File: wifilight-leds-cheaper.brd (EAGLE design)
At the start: 50.8 x 50.8 mm, 51 parts, among them Q1 BUK98180-100A, Q2 BUK98180-100A, Q3 BUK98180-100A, Q4 BUK98180-100A, U2 PCA9685

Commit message: add GPIO2 pins pogopins for programming
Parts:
- added TPCHPD, TPGPIO2: TEST-POINT3X5, SparkFun-Passives:PAD.03X.05
- moved TPGPIO0 1.11 mm to (26.2, 27.6)
- moved R5 0.16 mm to (28.4, 34.8)
- moved R6 0.16 mm to (30.5, 34.8)
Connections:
- removed net N$27: MPU.11
- removed net N$34: MPU.3
- new net CH_PD: MPU.11, TPCHPD.P$1
- new net GPIO2: MPU.3, TPGPIO2.P$1
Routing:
- net GPIO2: track 0.00 -> 21.0 mm
- net 3.3V: track 102.4 -> 106.3 mm, vias 5 -> 6
- net CH_PD: track 0.00 -> 2.32 mm
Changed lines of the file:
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@@
 <elements>
 <element name="C1" library="resistor" package="C0805K" value="0.1uF" x="38.57625" y="22.225" rot="MR270"/>
-<element name="R5" library="resistor" package="R0805" value="1k" x="28.41625" y="34.6075" rot="MR90"/>
-<element name="R6" library="resistor" package="R0805" value="1k" x="30.48" y="34.6075" rot="MR90"/>
+<element name="R5" library="resistor" package="R0805" value="1k" x="28.41625" y="34.76625" rot="MR90"/>
+<element name="R6" library="resistor" package="R0805" value="1k" x="30.48" y="34.76625" rot="MR90"/>
 <element name="U2" library="adafruit" package="TSSOP28" value="PCA9685" x="36.5125" y="23.1775"/>
 <element name="LED1" library="led" package="OVSTRGBBCR8" value="OVSTRGBBCR8" x="10.31875" y="33.9725" rot="MR120"/>
@@
 <element name="TPTX" library="SparkFun-Passives" package="PAD.03X.05" value="TEST-POINT3X5" x="18.25625" y="26.3525"/>
 <element name="TPRX" library="SparkFun-Passives" package="PAD.03X.05" value="TEST-POINT3X5" x="19.685" y="27.6225"/>
-<element name="TPGPIO0" library="SparkFun-Passives" package="PAD.03X.05" value="TEST-POINT3X5" x="25.0825" y="27.6225"/>
+<element name="TPGPIO0" library="SparkFun-Passives" package="PAD.03X.05" value="TEST-POINT3X5" x="26.19375" y="27.6225"/>
+<element name="TPCHPD" library="SparkFun-Passives" package="PAD.03X.05" value="TEST-POINT3X5" x="24.4475" y="27.6225"/>
+<element name="TPGPIO2" library="SparkFun-Passives" package="PAD.03X.05" value="TEST-POINT3X5" x="27.94" y="27.6225"/>
 </elements>
 <signals>
@@
 <wire x1="32.195" y1="29.68625" x2="32.195" y2="31.75" width="0.3048" layer="1"/>
 <via x="32.195" y="31.75" extent="1-16" drill="0.6"/>
-<wire x1="32.195" y1="31.75" x2="32.195" y2="31.9425" width="0.3048" layer="16"/>
-<wire x1="32.195" y1="31.9425" x2="30.48" y2="33.6575" width="0.3048" layer="16"/>
+<wire x1="32.195" y1="31.75" x2="32.195" y2="32.10125" width="0.3048" layer="16"/>
+<wire x1="32.195" y1="32.10125" x2="30.48" y2="33.81625" width="0.3048" layer="16"/>
 <contactref element="SCL" pad="P$1"/>
 <wire x1="29.68625" y1="23.33625" x2="29.68625" y2="21.9075" width="0.3048" layer="1"/>
@@
 <wire x1="30.195" y1="31.7175" x2="30.1625" y2="31.75" width="0.3048" layer="1"/>
 <via x="30.1625" y="31.75" extent="1-16" drill="0.6"/>
-<wire x1="30.1625" y1="31.75" x2="30.1625" y2="31.91125" width="0.3048" layer="16"/>
-<wire x1="30.1625" y1="31.91125" x2="28.41625" y2="33.6575" width="0.3048" layer="16"/>
+<wire x1="30.1625" y1="31.75" x2="30.1625" y2="32.07" width="0.3048" layer="16"/>
+<wire x1="30.1625" y1="32.07" x2="28.41625" y2="33.81625" width="0.3048" layer="16"/>
 <contactref element="SDA" pad="P$1"/>
 <wire x1="31.27375" y1="23.33625" x2="31.27375" y2="22.06625" width="0.3048" layer="1"/>
@@
 <wire x1="34.195" y1="31.75" x2="34.195" y2="32.86125" width="0.3048" layer="1"/>
 <wire x1="34.195" y1="32.86125" x2="32.385" y2="32.86125" width="0.3048" layer="1"/>
-<wire x1="29.21" y1="32.86125" x2="29.21" y2="27.46375" width="0.3048" layer="1"/>
-<wire x1="29.21" y1="27.46375" x2="29.21" y2="27.305" width="0.3048" layer="1"/>
+<wire x1="29.21" y1="32.86125" x2="29.21" y2="27.305" width="0.3048" layer="1"/>
 <wire x1="29.21" y1="27.305" x2="32.2875" y2="27.305" width="0.3048" layer="1"/>
 <wire x1="32.2875" y1="26.0953" x2="32.2875" y2="27.305" width="0.3048" layer="1"/>
@@
 <wire x1="12.90625" y1="28.575" x2="12.90625" y2="25.035" width="0.6096" layer="1"/>
 <wire x1="12.90625" y1="25.035" x2="13.49375" y2="24.4475" width="0.6096" layer="1"/>
-<wire x1="28.41625" y1="35.5575" x2="30.48" y2="35.5575" width="0.3048" layer="16"/>
+<wire x1="28.41625" y1="35.71625" x2="30.48" y2="35.71625" width="0.3048" layer="16"/>
 <wire x1="29.21" y1="32.86125" x2="32.385" y2="32.86125" width="0.3048" layer="1"/>
 <wire x1="32.385" y1="32.86125" x2="32.385" y2="34.29" width="0.3048" layer="1"/>
 <wire x1="32.385" y1="34.29" x2="32.0675" y2="34.6075" width="0.3048" layer="1"/>
 <via x="32.0675" y="34.6075" extent="1-16" drill="0.6"/>
-<wire x1="32.0675" y1="34.6075" x2="31.43" y2="34.6075" width="0.3048" layer="16"/>
-<wire x1="31.43" y1="34.6075" x2="30.48" y2="35.5575" width="0.3048" layer="16"/>
-<wire x1="21.11375" y1="27.46375" x2="21.11375" y2="24.92375" width="0.6096" layer="1"/>
-<wire x1="21.11375" y1="24.92375" x2="19.685" y2="24.92375" width="0.6096" layer="1"/>
+<wire x1="32.0675" y1="34.6075" x2="30.95375" y2="35.71875" width="0.3048" layer="16"/>
+<wire x1="30.95375" y1="35.71875" x2="30.48" y2="35.71625" width="0.3048" layer="16"/>
 <wire x1="19.685" y1="24.92375" x2="17.30375" y2="24.92375" width="0.6096" layer="1"/>
 <wire x1="17.30375" y1="24.92375" x2="16.98625" y2="25.24125" width="0.6096" layer="1"/>
@@
 <wire x1="17.4625" y1="41.5925" x2="12.90625" y2="28.575" width="0.6096" layer="1" curve="67.571913"/>
 <contactref element="TP3.3V" pad="P$1"/>
-<wire x1="21.11375" y1="27.46375" x2="23.01875" y2="27.46375" width="0.6096" layer="1"/>
-<wire x1="23.01875" y1="27.46375" x2="24.28875" y2="26.19375" width="0.6096" layer="1"/>
-<wire x1="24.28875" y1="26.19375" x2="26.51125" y2="26.19375" width="0.6096" layer="1"/>
-<wire x1="26.51125" y1="26.19375" x2="27.78125" y2="27.46375" width="0.6096" layer="1"/>
-<wire x1="27.78125" y1="27.46375" x2="29.21" y2="27.46375" width="0.6096" layer="1"/>
+<via x="29.21" y="27.305" extent="1-16" drill="0.6" shape="square"/>
+<wire x1="29.21" y1="27.305" x2="16.35125" y2="27.305" width="0.4064" layer="16"/>
+<wire x1="16.35125" y1="27.305" x2="13.49375" y2="24.4475" width="0.4064" layer="16"/>
 </signal>
 <signal name="N$13">
@@
 <contactref element="MPU" pad="12"/>
 </signal>
-<signal name="N$27">
+<signal name="CH_PD">
 <contactref element="MPU" pad="11"/>
+<contactref element="TPCHPD" pad="P$1"/>
+<wire x1="24.4475" y1="27.6225" x2="24.195" y2="27.6225" width="0.4064" layer="1"/>
+<wire x1="24.195" y1="27.6225" x2="24.195" y2="29.68625" width="0.4064" layer="1"/>
 </signal>
 <signal name="N$28">
@@
 <contactref element="MPU" pad="4"/>
 <contactref element="TPGPIO0" pad="P$1"/>
-<wire x1="25.0825" y1="27.6225" x2="25.0825" y2="36.195" width="0.3048" layer="1"/>
-<wire x1="25.0825" y1="36.195" x2="28.195" y2="39.3075" width="0.3048" layer="1"/>
-<wire x1="28.195" y1="45.88625" x2="28.195" y2="39.3075" width="0.3048" layer="1"/>
-</signal>
-<signal name="N$34">
+<wire x1="26.19375" y1="27.6225" x2="25.24125" y2="28.575" width="0.3048" layer="1"/>
+<wire x1="25.24125" y1="28.575" x2="25.24125" y2="37.1475" width="0.3048" layer="1"/>
+<wire x1="25.24125" y1="37.1475" x2="28.195" y2="40.10125" width="0.3048" layer="1"/>
+<wire x1="28.195" y1="45.88625" x2="28.195" y2="40.10125" width="0.3048" layer="1"/>
+</signal>
+<signal name="GPIO2">
 <contactref element="MPU" pad="3"/>
+<contactref element="TPGPIO2" pad="P$1"/>
+<wire x1="27.94" y1="27.6225" x2="27.14625" y2="28.41625" width="0.3048" layer="1"/>
+<wire x1="27.14625" y1="28.41625" x2="27.14625" y2="31.115" width="0.3048" layer="1"/>
+<wire x1="27.14625" y1="31.115" x2="25.7175" y2="32.54375" width="0.3048" layer="1"/>
+<wire x1="25.7175" y1="32.54375" x2="25.7175" y2="36.83" width="0.3048" layer="1"/>
+<wire x1="25.7175" y1="36.83" x2="30.083125" y2="41.195625" width="0.3048" layer="1"/>
+<wire x1="30.083125" y1="41.195625" x2="30.1625" y2="41.275" width="0.3048" layer="1"/>
+<wire x1="30.195" y1="45.88625" x2="30.195" y2="41.3075" width="0.3048" layer="1"/>
+<wire x1="30.195" y1="41.3075" x2="30.1625" y2="41.275" width="0.3048" layer="1"/>
 </signal>
 <signal name="N$36">

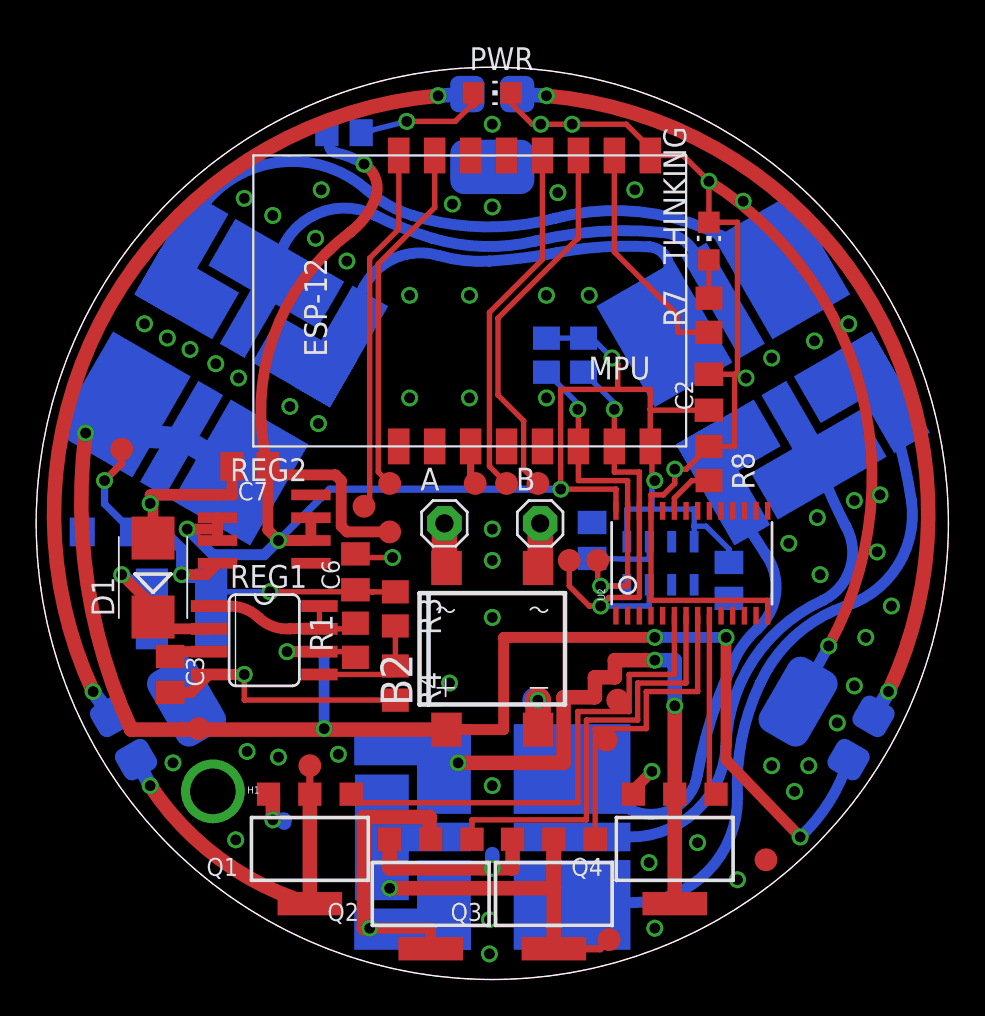
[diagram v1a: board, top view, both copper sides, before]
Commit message: Swapped to using 12x Luxeon Rebels instead of the hard-to-solder consolidated package.
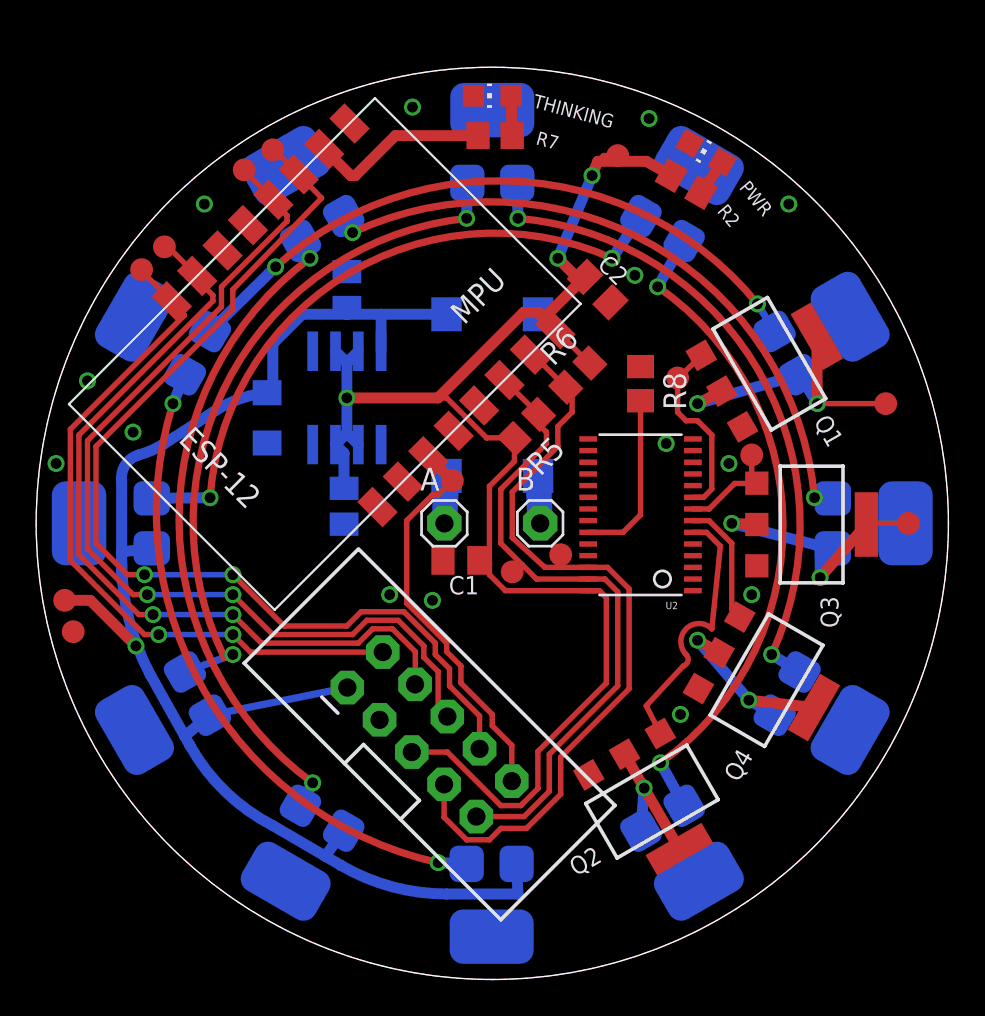
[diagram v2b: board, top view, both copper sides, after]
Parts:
- removed C3: 220pf, resistor:C0805K
- removed C4: 0.1uF, resistor:C0805K
- removed D1: MBRS140T3, diode:SMB
- removed H1: SEW_HOLE, LilyPad-Wearables:SIMPLE_HOLE
- removed L1: 220uf, SparkFun-Passives:SDR0403
- removed LED1, LED2, LED3: OVSTRGBBCR8, led:OVSTRGBBCR8
- removed R1: 220 ???, resistor:R0805
- removed R3: 3K, resistor:R0805
- removed R4: 1K, resistor:R0805
- removed REG1: MC33063/MC34063D, adafruit:SO08
- removed TEMPERATURE: MPL3115A2LGA8, SparkFun-Sensors:LGA8
- removed TP5V: TEST-POINT3X5, SparkFun-Passives:PAD.03X.05
- removed U$1, U$2, U$3: LUXEON-REBEL, SparkFun-LED:LUXEON-REBEL
- added BL1, BL2, BL3, GL1, GL2, GL3, RL1, RL2, RL3, WL1, WL2, WL3: LUXEON-REBEL, SparkFun-LED:LUXEON-REBEL
- added JP2: (no value), SparkFun-Connectors:2X5-SHROUDED_LOCK
- moved TPGND 40.6 mm to (2.06, 19.4)
- moved P_WHITE 37.9 mm to (47.3, 32.1)
- moved Q1 37.2 mm to (40.8, 34.3), turned to 300 degrees
- moved P_RED 28.5 mm to (48.6, 25.4)
- moved Q3 25.1 mm to (43.2, 25.3), turned to 270 degrees
- moved TP3.3V 24.5 mm to (32.4, 45.9)
- moved TPGPIO2 23.7 mm to (13.2, 46.2)
- moved TPGPIO0 22.8 mm to (11.6, 45.1)
- moved R2 19.3 mm to (36.2, 44.3), flipped to the top, turned to 330 degrees
- moved WHITE 18.2 mm to (35.7, 33.5)
- moved TPRX 18.2 mm to (7.14, 40.8)
- moved TPTX 18.1 mm to (5.87, 39.5)
- moved RED 17.8 mm to (39.8, 29.2)
- moved C6 15.7 mm to (17.3, 38.4), flipped to the bottom
- moved R7 15.5 mm to (25.6, 47.0), turned to 0 degrees
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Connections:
- net N$20 renamed #OE
- removed net 5V: C5.A, C6.1, L1.P$1, R3.1, REG2.4, TP5V.P$1
- removed net COMP: R3.2, R4.1, REG1.5
- removed net N$1: LED1.4, LED1.4@1, LED2.1
- removed net N$10: U$1.CATHODE, U$2.ANODE
- removed net N$11: U$2.CATHODE, U$3.ANODE
- removed net N$13: R1.2, REG1.1, REG1.7, REG1.8
- removed net N$16: C3.1, REG1.3
- removed net N$17: C4.1, TEMPERATURE.2
- removed net N$2: LED2.4, LED2.4@1, LED3.1
- removed net N$5: LED2.5, LED2.5@1, LED3.2
- removed net N$6: LED1.5, LED1.5@1, LED2.2
- removed net N$7: LED1.6, LED1.6@1, LED2.3
- removed net N$8: LED2.6, LED2.6@1, LED3.3
- removed net SWE: D1.C, L1.P$2, REG1.2
- new net B1: BL2.ANODE, BL3.CATHODE
- new net B2: BL1.ANODE, BL2.CATHODE
- new net G1: GL2.ANODE, GL3.CATHODE
- new net G2: GL1.ANODE, GL2.CATHODE
- new net R1: RL2.ANODE, RL3.CATHODE
- new net R2: RL1.ANODE, RL2.CATHODE
- new net W1: WL2.ANODE, WL3.CATHODE
- new net W2: WL1.ANODE, WL2.CATHODE
- net 12V: now also BL3.ANODE, C5.A, C6.1, GL3.ANODE, JP2.1, REG2.4, RL3.ANODE, WL3.ANODE; no longer LED1.1, LED1.2, LED1.3, R1.1, REG1.6, U$1.ANODE
- net 3.3V: now also JP2.5; no longer TEMPERATURE.1, TEMPERATURE.4
- net BLUE: now also U2.6; no longer U2.7
- net CH_PD: now also JP2.10
- net GND: now also BL1.P$3, BL2.P$3, BL3.P$3, GL1.P$3, GL2.P$3, GL3.P$3, JP2.3, RL1.P$3, RL2.P$3, RL3.P$3, WL1.P$3, WL2.P$3, WL3.P$3; no longer C3.2, C4.2, D1.A, H1.P$1, R4.2, REG1.4, TEMPERATURE.3, U$1.P$3, U$2.P$3, U$3.P$3
- net GPIO0: now also JP2.6
- net GPIO2: now also JP2.8
- net GREEN: now also U2.7; no longer U2.9
- net P_BLUE: now also BL1.CATHODE; no longer LED3.6, LED3.6@1
- net P_GREEN: now also GL1.CATHODE; no longer LED3.4, LED3.4@1
- net P_RED: now also RL1.CATHODE; no longer LED3.5, LED3.5@1
- net P_WHITE: now also WL1.CATHODE; no longer U$3.CATHODE
- net RXD: now also JP2.4
- net SCL: now also JP2.7; no longer TEMPERATURE.7
- net SDA: now also JP2.9; no longer TEMPERATURE.8
- net TXD: now also JP2.2
- net WHITE: now also U2.9; no longer U2.6
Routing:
- net GND: track 129.1 -> 0.00 mm, vias 70 -> 14
- net N$11: track 41.7 -> 0.00 mm, vias 2 -> 0
- net N$10: track 41.5 -> 0.00 mm, vias 2 -> 0
- net N$8: track 37.7 -> 0.00 mm
- net GPIO2: track 21.0 -> 57.0 mm, vias 0 -> 2
- net N$7: track 34.9 -> 0.00 mm
- net W2: track 0.00 -> 33.9 mm, vias 0 -> 2
- net G1: track 0.00 -> 33.2 mm, vias 0 -> 2
- net GPIO0: track 19.9 -> 52.8 mm, vias 0 -> 2
- net W1: track 0.00 -> 32.8 mm, vias 0 -> 2
- net B2: track 0.00 -> 32.2 mm, vias 0 -> 2
- net B1: track 0.00 -> 32.1 mm, vias 0 -> 2
- net G2: track 0.00 -> 31.9 mm, vias 0 -> 2
- net R1: track 0.00 -> 31.8 mm, vias 0 -> 2
- net R2: track 0.00 -> 31.7 mm, vias 0 -> 2
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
